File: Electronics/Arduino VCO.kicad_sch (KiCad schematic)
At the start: 39 parts, among them U1 TL072

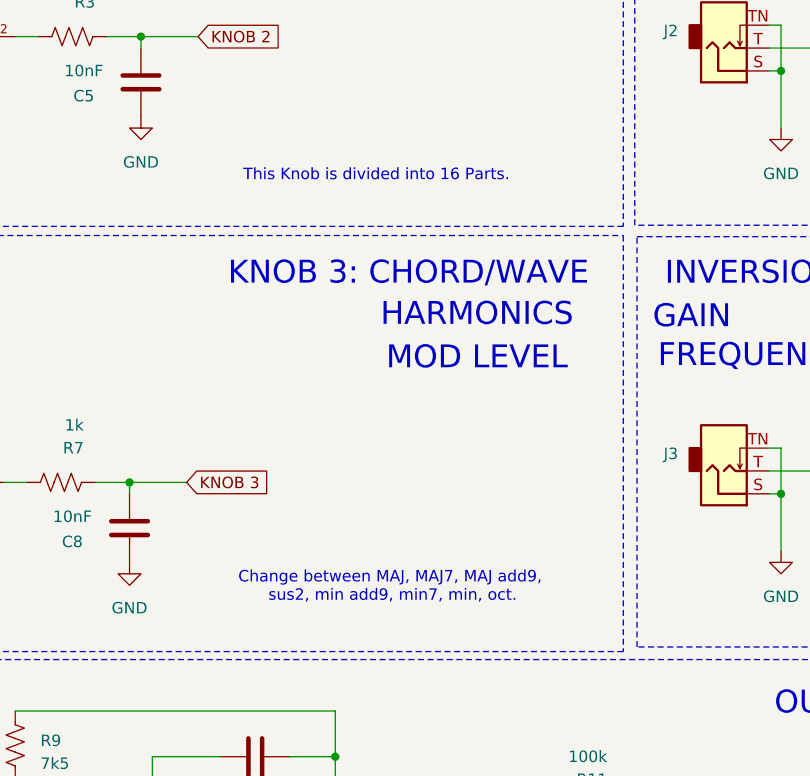
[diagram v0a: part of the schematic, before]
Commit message: deleting the plot
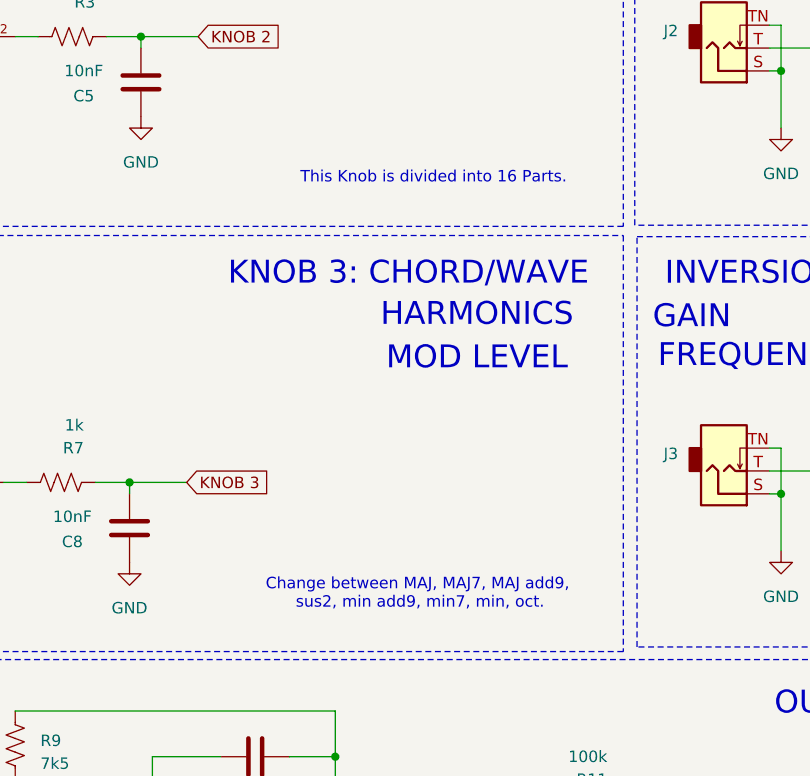
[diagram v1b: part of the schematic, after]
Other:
- company: Dirty Dream - Nathanael Noir -> ©Dirty Dream - Nathanael Noir
- title: Tripple VCO -> CY3-FOLD VCO
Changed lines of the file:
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@@
 	(paper "A4")
 	(title_block
-		(title "Tripple VCO")
-		(date "2026-04-15")
+		(title "CY3-FOLD VCO")
+		(date "2026-04-17")
 		(rev "v1.0")
-		(company "Dirty Dream - Nathanael Noir")
+		(company "©Dirty Dream - Nathanael Noir")
 	)
 	(rectangle
@@
 	(text "Change between MAJ, MAJ7, MAJ add9,\n sus2, min add9, min7, min, oct."
 		(exclude_from_sim no)
-		(at 74.676 145.034 0)
+		(at 77.724 145.796 0)
 		(effects
 			(font
@@
 	(text "This Knob is divided into 16 Parts. "
 		(exclude_from_sim no)
-		(at 73.152 99.314 0)
-		(effects
-			(font
+		(at 79.502 99.568 0)
+		(effects
+			(font

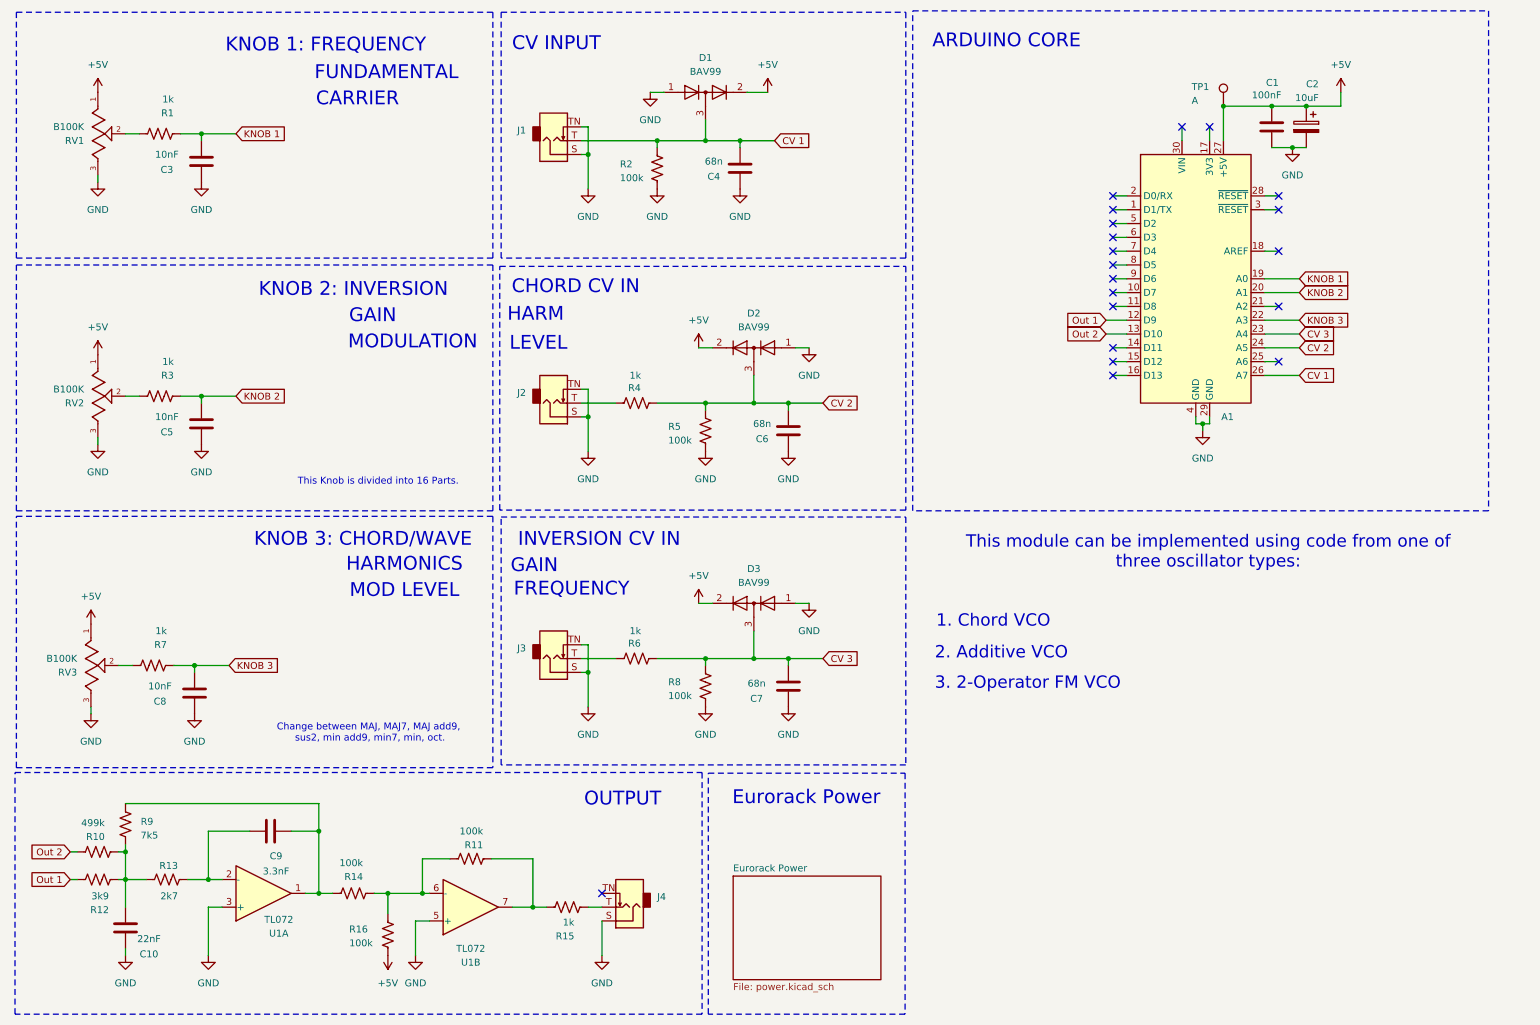
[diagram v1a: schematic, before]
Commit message: adding a comment for potental problem
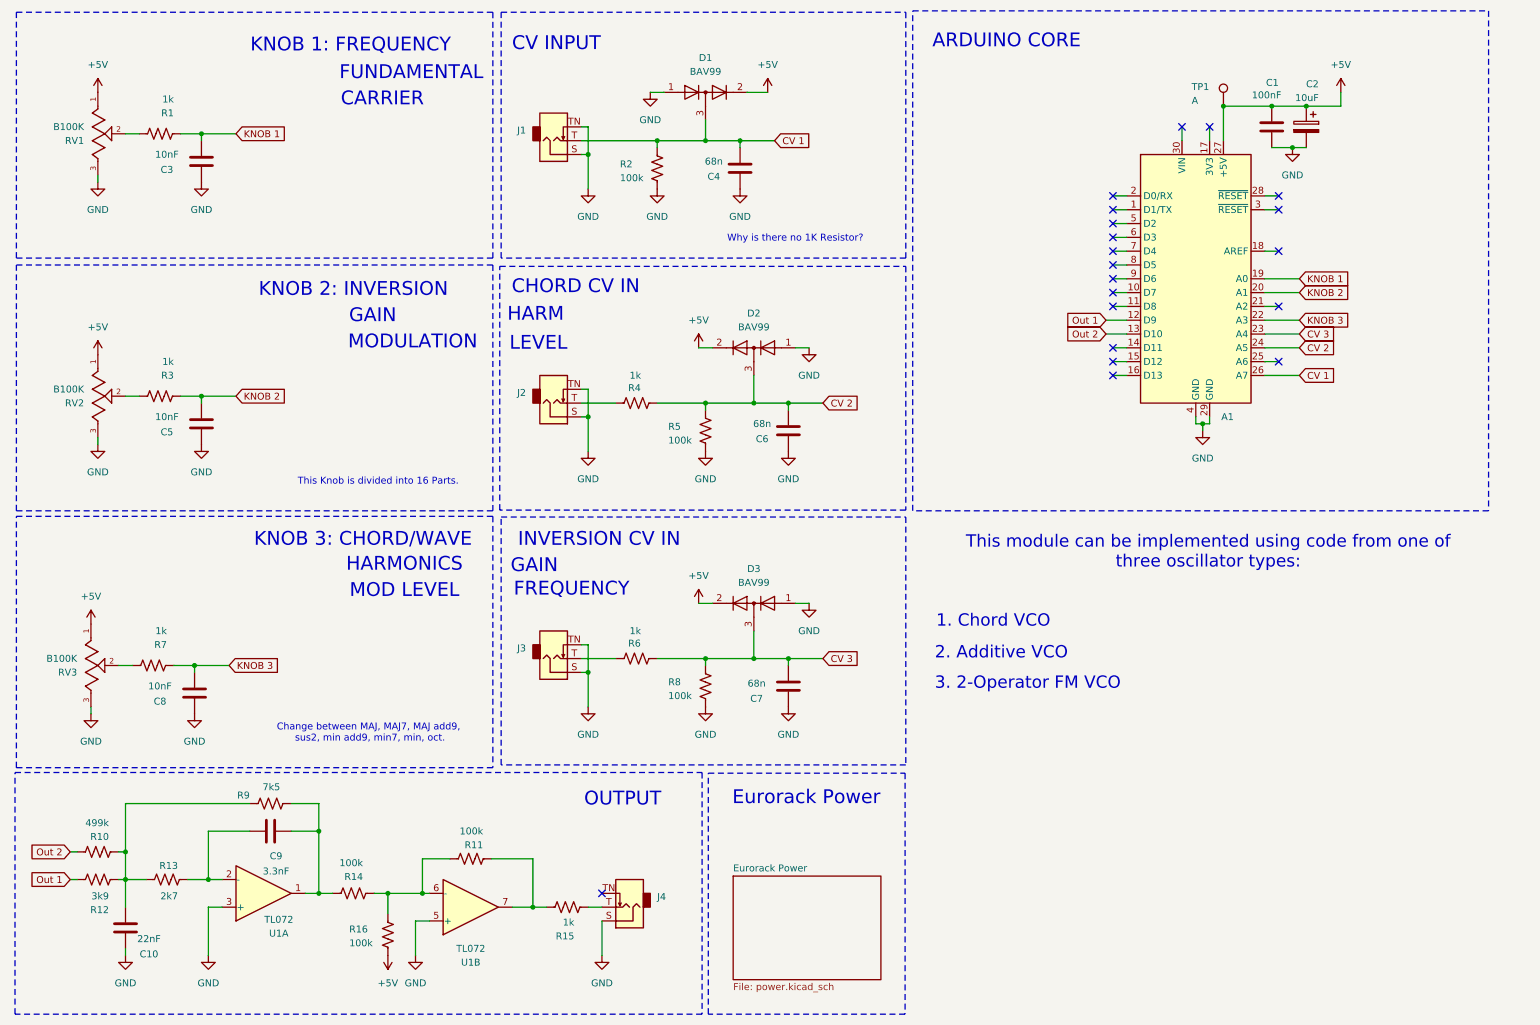
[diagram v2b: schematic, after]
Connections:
- net at C9.1, R14.1, U1.1: now also R9.1; no longer R9.2
- net at C10.1, R10.2, R12.2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: now also R9.2; no longer R9.1
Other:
- note added: "Why is there no 1K Resistor?"
- moved on the sheet: R9
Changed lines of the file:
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@@
 	(text "KNOB 1: FREQUENCY\n"
 		(exclude_from_sim no)
-		(at 69.85 19.304 0)
+		(at 74.422 19.304 0)
 		(effects
 			(font
@@
 	(text "FUNDAMENTAL\n"
 		(exclude_from_sim no)
-		(at 81.026 24.384 0)
+		(at 85.598 24.384 0)
 		(effects
 			(font
@@
 		)
 	)
+	(text "Why is there no 1K Resistor? "
+		(exclude_from_sim no)
+		(at 156.21 54.864 0)
+		(effects
+			(font
+				(size 1.27 1.27)
+				(color 255 0 0 1)
+			)
+		)
+	)
 	(text "1. Chord VCO"
 		(exclude_from_sim no)
@@
 	(text "CARRIER"
 		(exclude_from_sim no)
-		(at 75.692 29.21 0)
+		(at 80.264 29.21 0)
 		(effects
 			(font
@@
 	)
 	(junction
-		(at 33.02 167.64)
-		(diameter 0)
-		(color 0 0 0 0)
-	)
-	(junction
 		(at 231.14 88.9)
 		(diameter 0)
@@
 	)
 	(junction
+		(at 68.58 163.83)
+		(diameter 0)
+		(color 0 0 0 0)
+	)
+	(junction
 		(at 154.94 132.08)
 		(diameter 0)
@@
 	)
 	(junction
-		(at 68.58 163.83)
+		(at 118.11 134.62)
 		(diameter 0)
 		(color 0 0 0 0)
 	)
 	(junction
-		(at 118.11 134.62)
+		(at 33.02 172.72)
 		(diameter 0)
 		(color 0 0 0 0)
 	)
 	(junction
-		(at 33.02 172.72)
+		(at 33.02 167.64)
 		(diameter 0)
 		(color 0 0 0 0)
@@
 	(wire
 		(pts
+			(xy 33.02 158.75) (xy 33.02 167.64)
+		)
+		(stroke
+			(width 0)
+			(type default)
+		)
+	)
+	(wire
+		(pts
 			(xy 46.99 35.56) (xy 53.34 35.56)
 		)
@@
 	(wire
 		(pts
-			(xy 33.02 158.75) (xy 68.58 158.75)
+			(xy 33.02 158.75) (xy 55.88 158.75)
 		)
 		(stroke
@@
 	(wire
 		(pts
-			(xy 33.02 166.37) (xy 33.02 167.64)
-		)
-		(stroke
-			(width 0)
-			(type default)
-		)
-	)
-	(wire
-		(pts
 			(xy 214.63 77.47) (xy 217.17 77.47)
 		)
@@
 	(wire
 		(pts
+			(xy 63.5 158.75) (xy 68.58 158.75)
+		)
+		(stroke
+			(width 0)
+			(type default)
+		)
+	)
+	(wire
+		(pts
 			(xy 81.28 175.26) (xy 81.28 179.07)
 		)
@@
 	(symbol
 		(lib_id "Device:R_US")
-		(at 33.02 162.56 180)
+		(at 59.69 158.75 270)
 		(unit 1)
 		(body_style 1)
@@
 		(dnp no)
 		(property "Reference" "R9"
-			(at 35.814 162.052 0)
+			(at 55.88 157.226 90)
 			(show_name no)
 			(do_not_autoplace no)
@@
 		)
 		(property "Value" "7k5"
-			(at 35.814 164.592 0)
+			(at 61.468 155.702 90)
 			(show_name no)
 			(do_not_autoplace no)
@@
 		)
 		(property "Footprint" "Resistor_SMD:R_0805_2012Metric_Pad1.20x1.40mm_HandSolder"
-			(at 32.004 162.306 90)
+			(at 59.436 159.766 90)
 			(hide yes)
 			(show_name no)
@@
 		)
 		(property "Datasheet" ""
-			(at 33.02 162.56 0)
+			(at 59.69 158.75 0)
 			(hide yes)
 			(show_name no)
@@
 		)
 		(property "Description" "Resistor, US symbol"
-			(at 33.02 162.56 0)
+			(at 59.69 158.75 0)
 			(hide yes)
 			(show_name no)
@@
 		(dnp no)
 		(property "Reference" "R10"
-			(at 29.21 164.846 90)
+			(at 29.972 164.846 90)
 			(show_name no)
 			(do_not_autoplace no)
@@
 		)
 		(property "Value" "499k"
-			(at 29.21 162.306 90)
+			(at 29.972 162.306 90)
 			(show_name no)
 			(do_not_autoplace no)

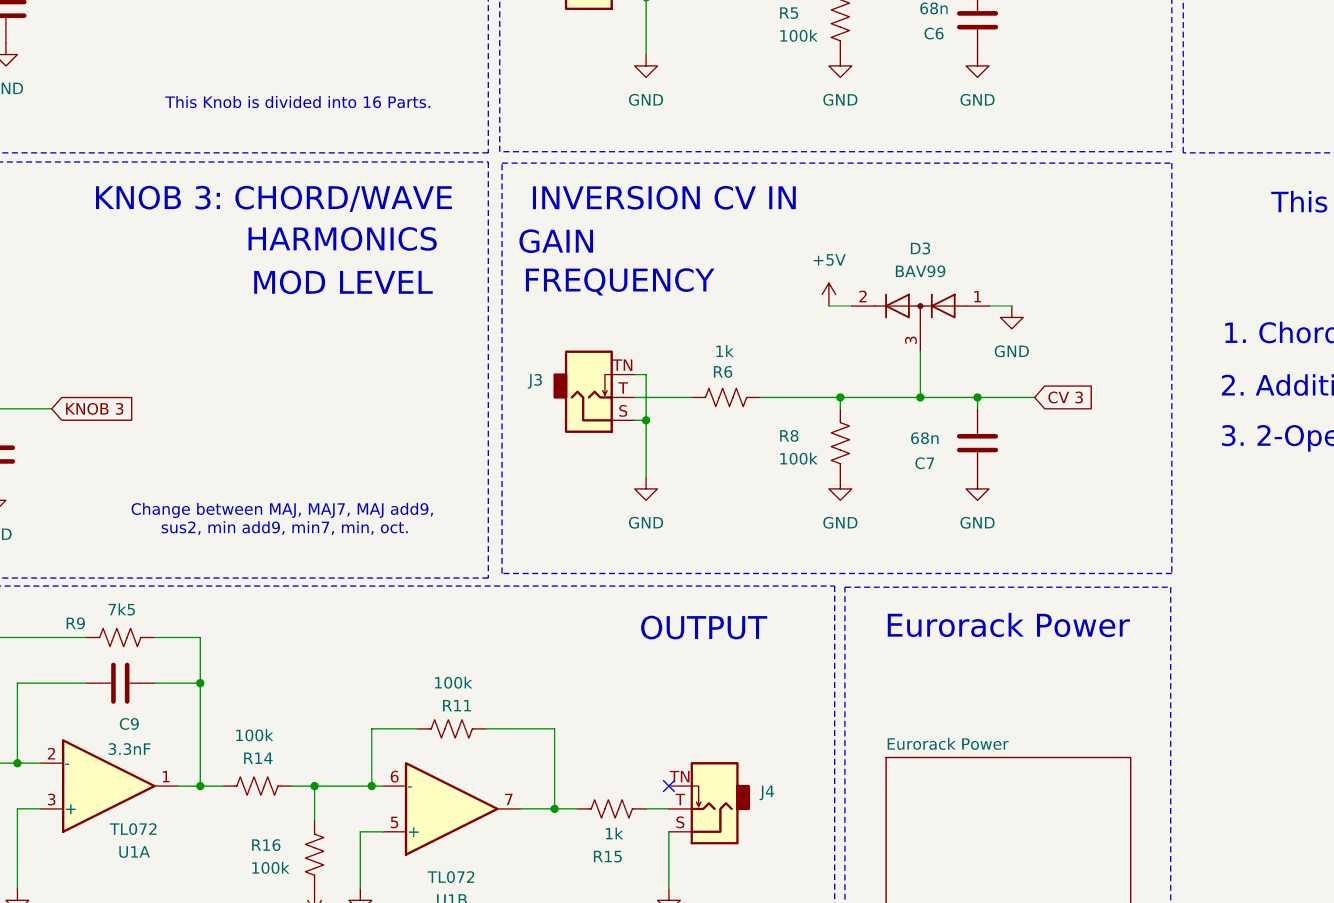
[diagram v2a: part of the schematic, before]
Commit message: optimized main_v1 reference
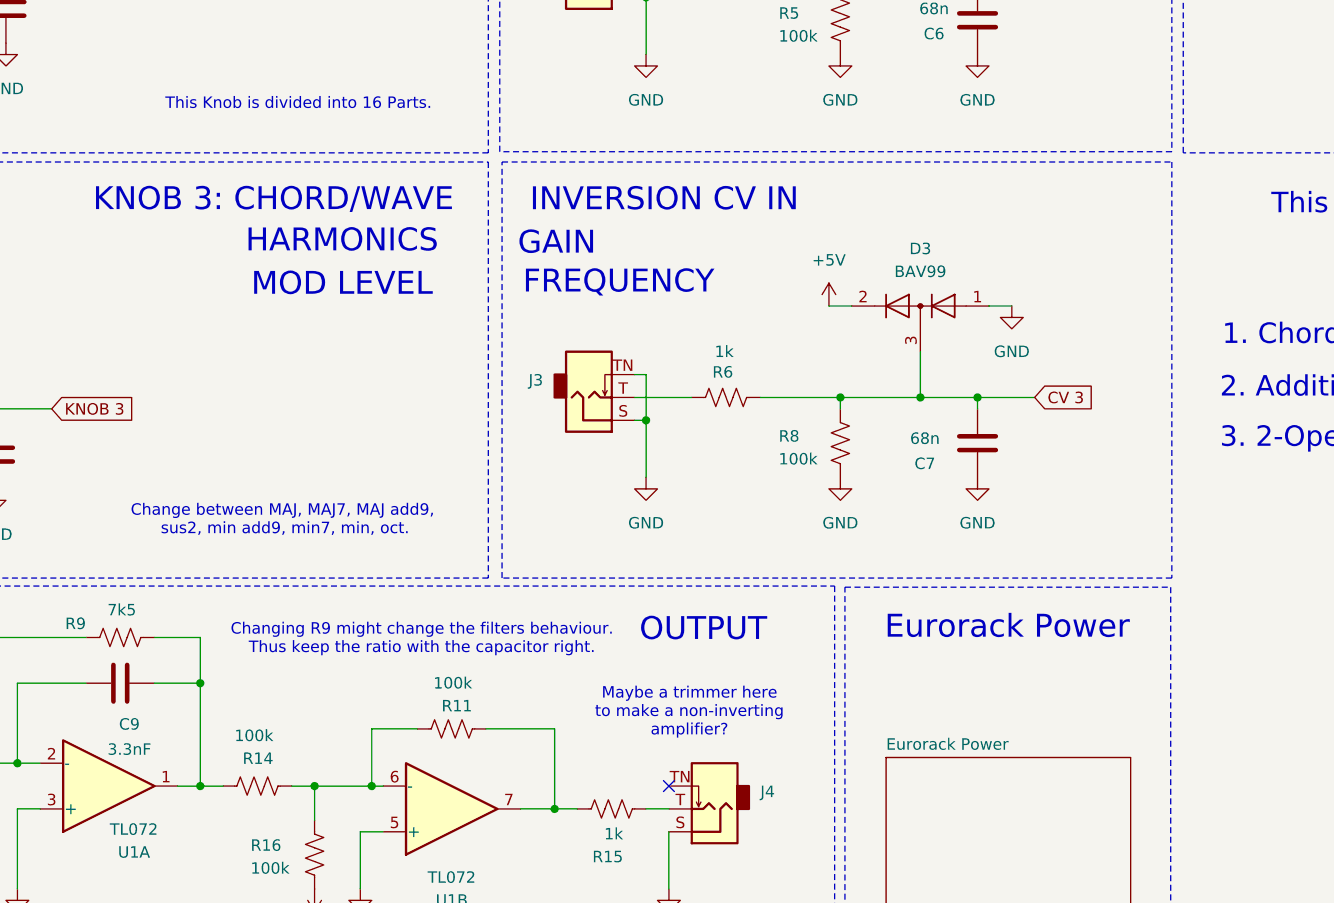
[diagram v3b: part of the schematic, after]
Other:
- note added: "Changing R9 might change the filters behaviour. Thus keep the ratio with the capacitor right."
- note added: "Maybe a trimmer here to make a non-inverting amplifier?"
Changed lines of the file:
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@@
 	)
 	(rectangle
-		(start 102.108 106.045)
-		(end 176.53 151.638)
+		(start 102.108 105.918)
+		(end 176.53 152.146)
 		(stroke
 			(width 0)
@@
 		)
 	)
+	(text "Maybe a trimmer here\nto make a non-inverting \namplifier?"
+		(exclude_from_sim no)
+		(at 122.936 167.132 0)
+		(effects
+			(font
+				(size 1.27 1.27)
+				(color 255 0 0 1)
+			)
+		)
+	)
 	(text ""
 		(exclude_from_sim no)
@@
 			)
 		)
+	)
+	(text "Changing R9 might change the filters behaviour. \nThus keep the ratio with the capacitor right."
+		(exclude_from_sim no)
+		(at 93.218 159.004 0)
+		(effects
+			(font
+				(size 1.27 1.27)
+				(color 255 0 0 1)
+			)
+		)
